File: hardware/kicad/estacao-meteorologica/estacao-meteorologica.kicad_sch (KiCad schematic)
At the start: 7 parts, among them J11 Conn_01x02_Socket, J4 Conn_cartao_SD, J5 Conn_BH1750, J6 Conn_BMP, U2 module_bh1750, U3 module_bme280, U6 MicroSD Card Adapter

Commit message: refatoracao: atualizacoes de hardware e falta revisao LoRa
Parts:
- removed J11: Conn_01x02_Socket, Connector_PinSocket_2.54mm:PinSocket_2x03_P2.54mm_Vertical, symbol Connector_Generic:Conn_02x03_Top_Bottom
- removed J4: Conn_cartao_SD, Connector_PinSocket_2.54mm:PinSocket_1x06_P2.54mm_Vertical, symbol Connector:Conn_01x06_Socket
- removed J5: Conn_BH1750, Connector_PinSocket_2.54mm:PinSocket_1x05_P2.54mm_Vertical, symbol Connector:Conn_01x05_Socket
- removed J6: Conn_BMP, Connector_PinSocket_2.54mm:PinSocket_1x06_P2.54mm_Vertical, symbol Connector:Conn_01x06_Socket
- removed U2: module_bh1750, myLibrary:bh1750_modulo, symbol biblioteca_modulos:module_bh1750
- removed U3: module_bme280, myLibrary:bme280_modulo, symbol biblioteca_modulos:module_bme280
- removed U6: MicroSD Card Adapter, myLibrary:Micro_SD_Card_Adapter, symbol Micro_SD_Card_Adapter:_MicroSD-Card-Adapter
- added H1, H2, H3, H4: MountingHole, symbol Mechanical:MountingHole
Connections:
- no-connect marks 0 -> 2
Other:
- sheet BH1750 ports: added I2C1_SCL, I2C1_SDA; removed none
- sheet BMP280 ports: added I2C1_SCL, I2C1_SDA; removed none
- sheet Cartao SD ports: added MCU_MOSI, SD_CD, SD_CS, SD_MISO, SD_SCK; removed none
- sheet DHT22 ports: added DHT_SIG; removed none
- sheet METEOROLOGIA ports: added AVREF_SENSOR; removed VREF_SENSOR
- sheet mcu ports: added AVREF_SENSOR, DHT_SIG, I2C1_SCL, I2C1_SDA, Lora_DIO0, Lora_DIO1, Lora_MISO, Lora_MOSI, Lora_NSS, Lora_RST, Lora_SCK, MCU_MOSI, SD_CS, SD_MISO, SD_SCK; removed VREF_SENSOR

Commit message: refatoracao: lora + Verificacao projeto inteiro
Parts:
- H1, H2, H3, H4: value MountingHole -> Furo M3 / Ø3,2 mm; footprint (none) -> MountingHole:MountingHole_3.2mm_M3; Assembly (none) -> Não comprar — recurso fabricado diretamente na PCB.; Function (none) -> Fixação mecânica da PCB ao gabinete ou espaçadores M3.; LCSC (none) -> N/A; LCSC Part (none) -> N/A; MPN (none) -> N/A — recurso mecânico da PCB; Manufacturer (none) -> N/A; Modelo 3D (none) -> N/A — um furo NPTH não possui corpo físico 3D; o parafuso/e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; Status_Ficha (none) -> Conferido: não entra na BOM. Validar posição, keepout e alt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
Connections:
- no-connect marks 2 -> 1
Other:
- sheet mcu ports: added Lora_DIO2; removed none

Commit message: Padronizacao de nomes e numero de componentes
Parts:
- H901: renamed from H1; value Furo M3 / Ø3,2 mm -> M3 NPTH, Ø3.2 mm; LCSC Part N/A -> (none); Modelo 3D N/A — um furo NPTH não possui corpo físico 3D; o parafuso/e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 -> (none); Specification (none) -> M3 NPTH, Ø3.2 mm; Status_Ficha Conferido: não entra na BOM. Validar posição, keepout e alt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 -> (none); Verification (none) -> Conferido: não entra na BOM. Validar posição, keepout e alt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
- H902: renamed from H2; value Furo M3 / Ø3,2 mm -> M3 NPTH, Ø3.2 mm; LCSC Part N/A -> (none); Modelo 3D N/A — um furo NPTH não possui corpo físico 3D; o parafuso/e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 -> (none); Specification (none) -> M3 NPTH, Ø3.2 mm; Status_Ficha Conferido: não entra na BOM. Validar posição, keepout e alt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 -> (none); Verification (none) -> Conferido: não entra na BOM. Validar posição, keepout e alt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
- H903: renamed from H3; value Furo M3 / Ø3,2 mm -> M3 NPTH, Ø3.2 mm; LCSC Part N/A -> (none); Modelo 3D N/A — um furo NPTH não possui corpo físico 3D; o parafuso/e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 -> (none); Specification (none) -> M3 NPTH, Ø3.2 mm; Status_Ficha Conferido: não entra na BOM. Validar posição, keepout e alt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 -> (none); Verification (none) -> Conferido: não entra na BOM. Validar posição, keepout e alt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
- H904: renamed from H4; value Furo M3 / Ø3,2 mm -> M3 NPTH, Ø3.2 mm; LCSC Part N/A -> (none); Modelo 3D N/A — um furo NPTH não possui corpo físico 3D; o parafuso/e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 -> (none); Specification (none) -> M3 NPTH, Ø3.2 mm; Status_Ficha Conferido: não entra na BOM. Validar posição, keepout e alt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 -> (none); Verification (none) -> Conferido: não entra na BOM. Validar posição, keepout e alt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
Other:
- sheet BH1750 renamed SENSOR BH1750
- sheet BMP280 renamed SENSOR BMP280
- sheet Cartao SD renamed CARTÃO microSD
- sheet DHT22 renamed SENSOR DHT22
- sheet LORA Module renamed RÁDIO LoRa
- sheet METEOROLOGIA renamed INTERFACES METEOROLÓGICAS
- sheet alimentacao renamed ALIMENTAÇÃO
- sheet mcu renamed MCU E DEPURAÇÃO
- sheet CARTÃO microSD ports: added SD_SPI_CS, SD_SPI_MOSI; removed MCU_MOSI, SD_CS
- sheet MCU E DEPURAÇÃO ports: added DHT22_DATA, LORA_DIO0, LORA_DIO1, LORA_DIO2, LORA_NSS, LORA_RST, LORA_SPI_MISO, LORA_SPI_MOSI, LORA_SPI_SCK, SD_SPI_CS, SD_SPI_MOSI; removed DHT_SIG, Lora_DIO0, Lora_DIO1, Lora_DIO2, Lora_MISO, Lora_MOSI, Lora_NSS, Lora_RST, Lora_SCK, MCU_MOSI, SD_CS
- sheet RÁDIO LoRa: file sheets/Lora_module.kicad_sch -> sheets/lora.kicad_sch
- sheet RÁDIO LoRa ports: added LORA_DIO0, LORA_DIO1, LORA_DIO2, LORA_NSS, LORA_RST, LORA_SPI_MISO, LORA_SPI_MOSI, LORA_SPI_SCK; removed Lora_DIO0, Lora_DIO1, Lora_DIO2, Lora_MISO, Lora_MOSI, Lora_NSS, Lora_RST, Lora_SCK
- sheet SENSOR BMP280: file sheets/untitled.kicad_sch -> sheets/bmp280.kicad_sch
- sheet SENSOR DHT22: file sheets/Dht22.kicad_sch -> sheets/dht22.kicad_sch
- sheet SENSOR DHT22 ports: added DHT22_DATA; removed DHT_SIG

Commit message: Ajuste de componentes por folha
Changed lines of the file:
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@@
 	(wire
 		(pts
-			(xy 78.74 30.48) (xy 88.9 30.48)
+			(xy 78.74 30.48) (xy 93.98 30.48)
 		)
 		(stroke
@@
 			(width 0)
 			(type default)
-		)
-	)
-	(global_label "+3V3"
-		(shape passive)
-		(at 88.9 30.48 0)
-		(effects
-			(font
-				(size 1.27 1.27)
-			)
-			(justify left)
-		)
-		(property "Intersheetrefs" "${INTERSHEET_REFS}"
-			(at 88.9 30.48 0)
-			(effects
-				(font
-					(size 1.27 1.27)
-				)
-				(hide yes)
-			)
-		)
-	)
-	(global_label "+5V"
-		(shape passive)
-		(at 88.9 25.4 0)
-		(effects
-			(font
-				(size 1.27 1.27)
-			)
-			(justify left)
-		)
-		(property "Intersheetrefs" "${INTERSHEET_REFS}"
-			(at 88.9 25.4 0)
-			(effects
-				(font
-					(size 1.27 1.27)
-				)
-				(hide yes)
-			)
 		)
 	)
@@
 		)
 	)
-	(global_label "GND"
-		(shape passive)
-		(at 88.9 35.56 0)
-		(effects
-			(font
-				(size 1.27 1.27)
-			)
-			(justify left)
-		)
-		(property "Intersheetrefs" "${INTERSHEET_REFS}"
-			(at 88.9 35.56 0)
-			(effects
-				(font
-					(size 1.27 1.27)
-				)
-				(hide yes)
-			)
-		)
-	)
 	(global_label "AVREF_SENSOR"
 		(shape passive)
@@
 				)
 				(hide yes)
+			)
+		)
+	)
+	(symbol
+		(lib_id "power:+5V")
+		(at 88.9 25.4 0)
+		(unit 1)
+		(exclude_from_sim no)
+		(in_bom yes)
+		(on_board yes)
+		(dnp no)
+		(fields_autoplaced yes)
+		(property "Reference" "#PWR080"
+			(at 88.9 29.21 0)
+			(effects
+				(font
+					(size 1.27 1.27)
+				)
+				(hide yes)
+			)
+		)
+		(property "Value" "+5V"
+			(at 88.9 20.32 0)
+			(effects
+				(font
+					(size 1.27 1.27)
+				)
+			)
+		)
+		(property "Footprint" ""
+			(at 88.9 25.4 0)
+			(effects
+				(font
+					(size 1.27 1.27)
+				)
+				(hide yes)
+			)
+		)
+		(property "Datasheet" ""
+			(at 88.9 25.4 0)
+			(effects
+				(font
+					(size 1.27 1.27)
+				)
+				(hide yes)
+			)
+		)
+		(property "Description" "Power symbol creates a global label with name \"+5V\""
+			(at 88.9 25.4 0)
+			(effects
+				(font
+					(size 1.27 1.27)
+				)
+				(hide yes)
+			)
+		)
+		(pin "1"
+		)
+		(instances
+			(project ""
+				(path "/0c305a6e-f9cd-49a1-b146-c2956e5469b6"
+					(reference "#PWR080")
+					(unit 1)
+				)
+			)
+		)
+	)
+	(symbol
+		(lib_id "power:+3V3")
+		(at 93.98 30.48 0)
+		(unit 1)
+		(exclude_from_sim no)
+		(in_bom yes)
+		(on_board yes)
+		(dnp no)
+		(fields_autoplaced yes)
+		(property "Reference" "#PWR079"
+			(at 93.98 34.29 0)
+			(effects
+				(font
+					(size 1.27 1.27)
+				)
+				(hide yes)
+			)
+		)
+		(property "Value" "+3V3"
+			(at 93.98 25.4 0)
+			(effects
+				(font
+					(size 1.27 1.27)
+				)
+			)
+		)
+		(property "Footprint" ""
+			(at 93.98 30.48 0)
+			(effects
+				(font
+					(size 1.27 1.27)
+				)
+				(hide yes)
+			)
+		)
+		(property "Datasheet" ""
+			(at 93.98 30.48 0)
+			(effects
+				(font
+					(size 1.27 1.27)
+				)
+				(hide yes)
+			)
+		)
+		(property "Description" "Power symbol creates a global label with name \"+3V3\""
+			(at 93.98 30.48 0)
+			(effects
+				(font
+					(size 1.27 1.27)
+				)
+				(hide yes)
+			)
+		)
+		(pin "1"
+		)
+		(instances
+			(project ""
+				(path "/0c305a6e-f9cd-49a1-b146-c2956e5469b6"
+					(reference "#PWR079")
+					(unit 1)
+				)
 			)
 		)
@@
 			)
 		)
+		(property "Specification" "M3 NPTH, Ø3.2 mm"
+			(at 0 0 0)
+			(effects
+				(font
+					(size 1.27 1.27)
+				)
+				(hide yes)
+			)
+		)
 		(instances
 			(project ""
@@
 					(unit 1)
 				)
-			)
-		)
-		(property "Specification" "M3 NPTH, Ø3.2 mm"
-			(at 0 0 0)
-			(effects
-				(font (size 1.27 1.27))
-				(hide yes)
 			)
 		)
@@
 			)
 		)
+		(property "Specification" "M3 NPTH, Ø3.2 mm"
+			(at 0 0 0)
+			(effects
+				(font
+					(size 1.27 1.27)
+				)
+				(hide yes)
+			)
+		)
 		(instances
 			(project ""
@@
 					(unit 1)
 				)
-			)
-		)
-		(property "Specification" "M3 NPTH, Ø3.2 mm"
-			(at 0 0 0)
-			(effects
-				(font (size 1.27 1.27))
-				(hide yes)
 			)
 		)
@@
 			)
 		)
+		(property "Specification" "M3 NPTH, Ø3.2 mm"
+			(at 0 0 0)
+			(effects
+				(font
+					(size 1.27 1.27)
+				)
+				(hide yes)
+			)
+		)
 		(instances
 			(project "estacao-meteorologica"
@@
 			)
 		)
-		(property "Specification" "M3 NPTH, Ø3.2 mm"
-			(at 0 0 0)
-			(effects
-				(font (size 1.27 1.27))
-				(hide yes)
+	)
+	(symbol
+		(lib_id "power:GND")
+		(at 88.9 35.56 0)
+		(unit 1)
+		(exclude_from_sim no)
+		(in_bom yes)
+		(on_board yes)
+		(dnp no)
+		(fields_autoplaced yes)
+		(property "Reference" "#PWR078"
+			(at 88.9 41.91 0)
+			(effects
+				(font
+					(size 1.27 1.27)
+				)
+				(hide yes)
+			)
+		)
+		(property "Value" "GND"
+			(at 88.9 40.64 0)
+			(effects
+				(font
+					(size 1.27 1.27)
+				)
+			)
+		)
+		(property "Footprint" ""
+			(at 88.9 35.56 0)
+			(effects
+				(font
+					(size 1.27 1.27)
+				)
+				(hide yes)
+			)
+		)
+		(property "Datasheet" ""
+			(at 88.9 35.56 0)
+			(effects
+				(font
+					(size 1.27 1.27)
+				)
+				(hide yes)
+			)
+		)
+		(property "Description" "Power symbol creates a global label with name \"GND\" , ground"
+			(at 88.9 35.56 0)
+			(effects
+				(font
+					(size 1.27 1.27)
+				)
+				(hide yes)
+			)
+		)
+		(pin "1"
+		)
+		(instances
+			(project ""
+				(path "/0c305a6e-f9cd-49a1-b146-c2956e5469b6"
+					(reference "#PWR078")
+					(unit 1)
+				)
 			)
 		)
@@
 			)
 		)
+		(property "Specification" "M3 NPTH, Ø3.2 mm"
+			(at 0 0 0)
+			(effects
+				(font
+					(size 1.27 1.27)
+				)
+				(hide yes)
+			)
+		)
 		(instances
 			(project "estacao-meteorologica"
@@
 			)
 		)
-		(property "Specification" "M3 NPTH, Ø3.2 mm"
-			(at 0 0 0)
-			(effects
-				(font (size 1.27 1.27))
-				(hide yes)
-			)
-		)

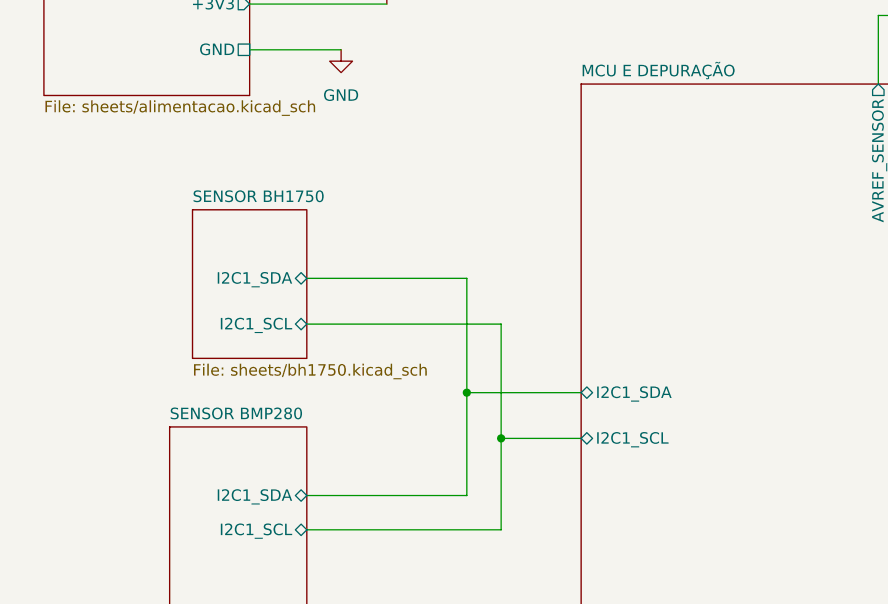
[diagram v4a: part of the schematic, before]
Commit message: Refact - mudança do sensor bh1750 para placa filha e conector jst + reposicionamento do sensor DHT22 para reduzir influencia de temperatura interna da placa
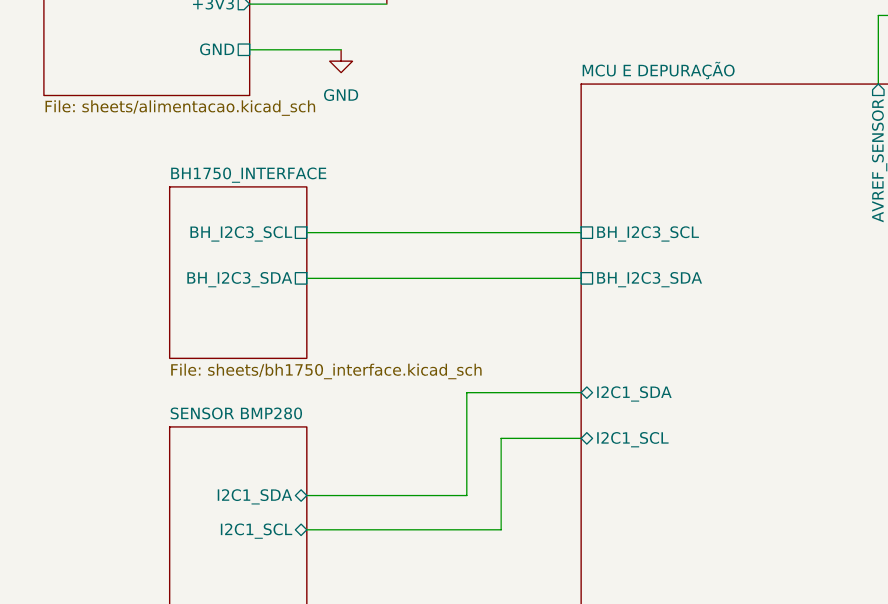
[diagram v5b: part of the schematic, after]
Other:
- removed sheet SENSOR BH1750
- added sheet BH1750_INTERFACE (sheets/bh1750_interface.kicad_sch)
- sheet MCU E DEPURAÇÃO ports: added BH_I2C3_SCL, BH_I2C3_SDA; removed none
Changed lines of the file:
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@@
 	(generator_version "9.0")
 	(paper "A4")
-	(junction
-		(at 106.68 78.74)
-		(diameter 0)
-		(color 0 0 0 0)
-	)
-	(junction
-		(at 102.87 73.66)
-		(diameter 0)
-		(color 0 0 0 0)
-	)
 	(no_connect
 		(at 210.82 125.73)
@@
 	(wire
 		(pts
-			(xy 106.68 66.04) (xy 106.68 78.74)
-		)
-		(stroke
-			(width 0)
-			(type default)
-		)
-	)
-	(wire
-		(pts
 			(xy 148.59 31.75) (xy 151.13 31.75)
 		)
@@
 	(wire
 		(pts
-			(xy 85.09 66.04) (xy 106.68 66.04)
-		)
-		(stroke
-			(width 0)
-			(type default)
-		)
-	)
-	(wire
-		(pts
 			(xy 85.09 85.09) (xy 102.87 85.09)
 		)
@@
 	(wire
 		(pts
-			(xy 85.09 60.96) (xy 102.87 60.96)
-		)
-		(stroke
-			(width 0)
-			(type default)
-		)
-	)
-	(wire
-		(pts
 			(xy 182.88 135.89) (xy 210.82 135.89)
 		)
@@
 	(wire
 		(pts
-			(xy 102.87 60.96) (xy 102.87 73.66)
-		)
-		(stroke
-			(width 0)
-			(type default)
-		)
-	)
-	(wire
-		(pts
 			(xy 85.09 88.9) (xy 106.68 88.9)
 		)
@@
 	(wire
 		(pts
+			(xy 85.09 55.88) (xy 115.57 55.88)
+		)
+		(stroke
+			(width 0)
+			(type default)
+		)
+	)
+	(wire
+		(pts
 			(xy 182.88 50.8) (xy 210.82 50.8)
+		)
+		(stroke
+			(width 0)
+			(type default)
+		)
+	)
+	(wire
+		(pts
+			(xy 85.09 60.96) (xy 115.57 60.96)
 		)
 		(stroke
@@
 			)
 		)
+		(pin "BH_I2C3_SCL" passive
+			(at 115.57 55.88 180)
+			(effects
+				(font
+					(size 1.27 1.27)
+				)
+				(justify left)
+			)
+		)
+		(pin "BH_I2C3_SDA" passive
+			(at 115.57 60.96 180)
+			(effects
+				(font
+					(size 1.27 1.27)
+				)
+				(justify left)
+			)
+		)
 		(instances
 			(project "estacao-meteorologica"
@@
 	)
 	(sheet
-		(at 72.39 53.34)
-		(size 12.7 16.51)
+		(at 69.85 50.8)
+		(size 15.24 19.05)
 		(exclude_from_sim no)
 		(in_bom yes)
@@
 			(color 0 0 0 0.0000)
 		)
-		(property "Sheetname" "SENSOR BH1750"
-			(at 72.39 52.6284 0)
+		(property "Sheetname" "BH1750_INTERFACE"
+			(at 69.85 50.0884 0)
 			(effects
 				(font
@@
 			)
 		)
-		(property "Sheetfile" "sheets/bh1750.kicad_sch"
-			(at 72.39 70.4346 0)
+		(property "Sheetfile" "sheets/bh1750_interface.kicad_sch"
+			(at 69.85 70.4346 0)
 			(effects
 				(font
@@
 			)
 		)
-		(pin "I2C1_SCL" bidirectional
-			(at 85.09 66.04 0)
-			(effects
-				(font
-					(size 1.27 1.27)
-				)
-				(justify right)
-			)
-		)
-		(pin "I2C1_SDA" bidirectional
+		(pin "BH_I2C3_SCL" passive
+			(at 85.09 55.88 0)
+			(effects
+				(font
+					(size 1.27 1.27)
+				)
+				(justify right)
+			)
+		)
+		(pin "BH_I2C3_SDA" passive
 			(at 85.09 60.96 0)
 			(effects
@@
 			(project "estacao-meteorologica"
 				(path "/0c305a6e-f9cd-49a1-b146-c2956e5469b6"
-					(page "5")
-				)
-			)
+					(page "12")
+				)
+			)

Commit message: Refact: tirei estagio de 12V -> 5V e agora é direto 12V -> 3V
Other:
- sheet ALIMENTAÇÃO ports: added none; removed +5V
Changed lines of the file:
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@@
-	(wire
-		(pts
-			(xy 78.74 25.4) (xy 88.9 25.4)
-		)
-		(stroke
-			(width 0)
-			(type default)
-		)
-	)
 	(wire
 		(pts
@@
 				)
 				(hide yes)
-			)
-		)
-	)
-	(symbol
-		(lib_id "power:+5V")
-		(at 88.9 25.4 0)
-		(unit 1)
-		(exclude_from_sim no)
-		(in_bom yes)
-		(on_board yes)
-		(dnp no)
-		(fields_autoplaced yes)
-		(property "Reference" "#PWR080"
-			(at 88.9 29.21 0)
-			(effects
-				(font
-					(size 1.27 1.27)
-				)
-				(hide yes)
-			)
-		)
-		(property "Value" "+5V"
-			(at 88.9 20.32 0)
-			(effects
-				(font
-					(size 1.27 1.27)
-				)
-			)
-		)
-		(property "Footprint" ""
-			(at 88.9 25.4 0)
-			(effects
-				(font
-					(size 1.27 1.27)
-				)
-				(hide yes)
-			)
-		)
-		(property "Datasheet" ""
-			(at 88.9 25.4 0)
-			(effects
-				(font
-					(size 1.27 1.27)
-				)
-				(hide yes)
-			)
-		)
-		(property "Description" "Power symbol creates a global label with name \"+5V\""
-			(at 88.9 25.4 0)
-			(effects
-				(font
-					(size 1.27 1.27)
-				)
-				(hide yes)
-			)
-		)
-		(pin "1"
-		)
-		(instances
-			(project ""
-				(path "/0c305a6e-f9cd-49a1-b146-c2956e5469b6"
-					(reference "#PWR080")
-					(unit 1)
-				)
 			)
 		)
@@
 			)
 		)
-		(pin "+5V" output
-			(at 78.74 25.4 0)
-			(effects
-				(font
-					(size 1.27 1.27)
-				)
-				(justify right)
-			)
-		)
